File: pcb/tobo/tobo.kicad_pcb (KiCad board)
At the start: 2 copper layers, 57.5 x 61 mm, 97 parts, among them J1 Molex 538-54548-2272, J2 Conn_01x02_Pin, J4 Molex 538-54548-2472, J5 Conn_01x09_Pin, J6 Conn_01x09_Pin, J7 Conn_01x09_Pin, J8 Hroparts Elec TYPE-C-31-M-12, U1 TS5A23167, U10 5015, U11 5015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

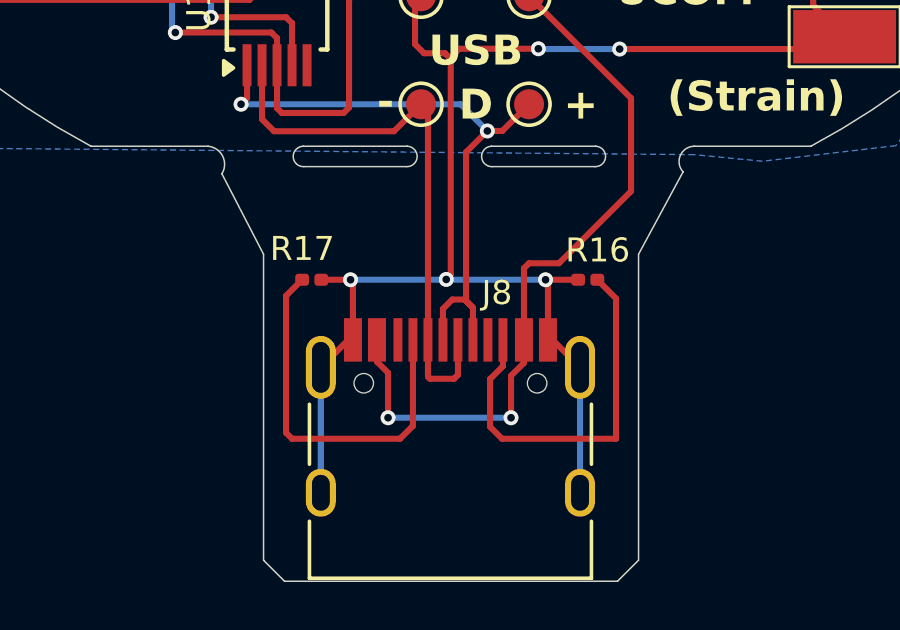
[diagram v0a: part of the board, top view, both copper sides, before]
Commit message: Cleared edges of USB board
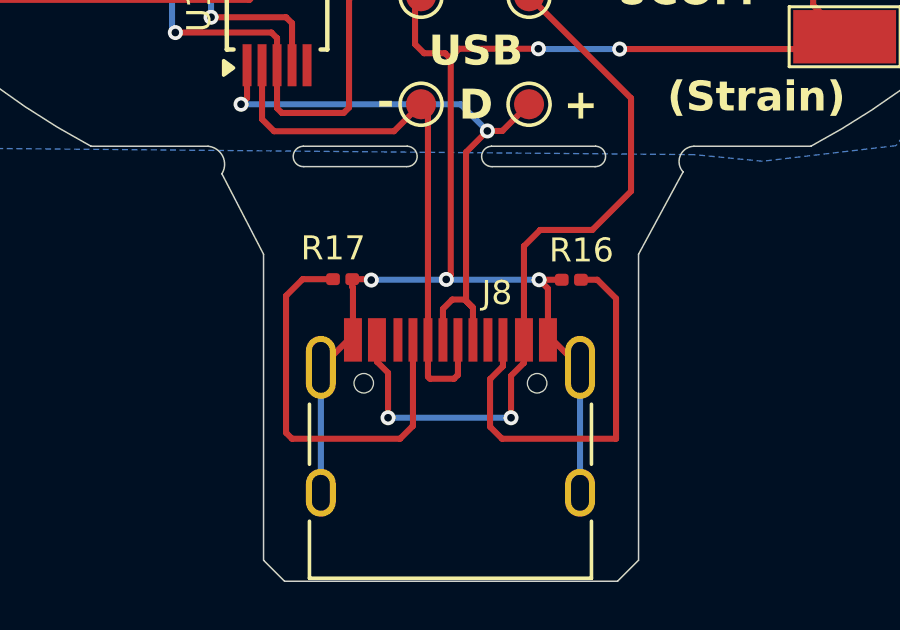
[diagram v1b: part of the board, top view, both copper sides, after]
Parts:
- moved R17 1.03 mm to (136.4, 116.9)
- moved R16 0.55 mm to (144.0, 117.0)
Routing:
- net GND: track 195.3 -> 193.8 mm
- net Net-(J8-CC1): track 12.7 -> 13.7 mm
- net Net-(J8-CC2): track 13.0 -> 13.5 mm
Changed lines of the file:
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@@
 	(footprint "Resistor_SMD:R_0201_0603Metric"
 		(layer "F.Cu")
-		(at 135.355 116.95)
+		(at 136.385 116.93)
 		(descr "Resistor SMD 0201 (0603 Metric), square (rectangular) end terminal, IPC_7351 nominal, (Body size source: https://www.vishay.com/docs/20052/crcw0201e3.pdf), generated with kicad-footprint-generator")
 		(tags "resistor")
@@
 	(footprint "Resistor_SMD:R_0201_0603Metric"
 		(layer "F.Cu")
-		(at 144.555 116.95 180)
+		(at 144.01 116.95 180)
 		(descr "Resistor SMD 0201 (0603 Metric), square (rectangular) end terminal, IPC_7351 nominal, (Body size source: https://www.vishay.com/docs/20052/crcw0201e3.pdf), generated with kicad-footprint-generator")
 		(tags "resistor")
@@
 	)
 	(segment
-		(start 136.73 118.955)
-		(end 136.73 117.03)
+		(start 136.705 117.185)
+		(end 136.705 116.93)
 		(width 0.2032)
 		(layer "F.Cu")
@@
 	)
 	(segment
+		(start 137.31 116.93)
+		(end 137.34 116.96)
+		(width 0.2032)
+		(layer "F.Cu")
+		(net 44)
+	)
+	(segment
 		(start 135.5 103.035)
 		(end 134.7 103.035)
@@
 	)
 	(segment
-		(start 135.675 116.95)
-		(end 136.65 116.95)
-		(width 0.2032)
-		(layer "F.Cu")
-		(net 44)
-	)
-	(segment
 		(start 131.11 78.63)
 		(end 145.849999 78.63)
@@
 	)
 	(segment
-		(start 136.73 117.03)
-		(end 136.65 116.95)
-		(width 0.2032)
-		(layer "F.Cu")
-		(net 44)
-	)
-	(segment
 		(start 136.7 107.5)
 		(end 139 107.5)
@@
 	(segment
 		(start 143.23 118.955)
-		(end 143.23 117.03)
+		(end 143.23 117.246)
 		(width 0.2032)
 		(layer "F.Cu")
@@
 	)
 	(segment
-		(start 153.12 108.85)
-		(end 152.71 109.26)
+		(start 142.934 116.95)
+		(end 143.69 116.95)
 		(width 0.2032)
 		(layer "F.Cu")
@@
 	)
 	(segment
-		(start 135.5 100.9)
-		(end 136.4 100)
+		(start 153.12 108.85)
+		(end 152.71 109.26)
 		(width 0.2032)
 		(layer "F.Cu")
@@
 	)
 	(segment
-		(start 144.235 116.95)
-		(end 143.15 116.95)
+		(start 135.5 100.9)
+		(end 136.4 100)
 		(width 0.2032)
 		(layer "F.Cu")
@@
 	)
 	(segment
+		(start 136.705 116.93)
+		(end 137.31 116.93)
+		(width 0.2032)
+		(layer "F.Cu")
+		(net 44)
+	)
+	(segment
 		(start 122.775 99.565)
 		(end 122.8 99.54)
@@
 	)
 	(segment
+		(start 136.73 118.955)
+		(end 136.73 117.21)
+		(width 0.2032)
+		(layer "F.Cu")
+		(net 44)
+	)
+	(segment
 		(start 122.035 84.8)
 		(end 122.035 85.7)
@@
 	)
 	(segment
-		(start 143.23 117.03)
-		(end 143.15 116.95)
-		(width 0.2032)
-		(layer "F.Cu")
-		(net 44)
-	)
-	(segment
 		(start 135.5 100.9)
 		(end 133.7 100.9)
@@
 	)
 	(segment
+		(start 143.23 117.246)
+		(end 142.934 116.95)
+		(width 0.2032)
+		(layer "F.Cu")
+		(net 44)
+	)
+	(segment
 		(start 133.9 103.035)
 		(end 134.7 103.035)
@@
 	)
 	(segment
+		(start 136.73 117.21)
+		(end 136.705 117.185)
+		(width 0.2032)
+		(layer "F.Cu")
+		(net 44)
+	)
+	(segment
 		(start 119.43 91.07)
 		(end 122 91.07)
@@
 	)
 	(via
-		(at 143.15 116.95)
+		(at 142.934 116.95)
 		(size 0.5)
 		(drill 0.254)
@@
 	)
 	(via
-		(at 136.65 116.95)
+		(at 137.34 116.96)
 		(size 0.5)
 		(drill 0.254)
@@
 	)
 	(segment
+		(start 137.34 116.96)
+		(end 137.35 116.95)
+		(width 0.2032)
+		(layer "B.Cu")
+		(net 44)
+	)
+	(segment
 		(start 135.5 100.9)
 		(end 135.5 101)
@@
 	)
 	(segment
-		(start 142.91 109.25)
-		(end 142.92 109.26)
+		(start 137.35 116.95)
+		(end 139.83 116.95)
 		(width 0.2032)
 		(layer "B.Cu")
@@
 	)
 	(segment
-		(start 143.15 116.95)
-		(end 139.85 116.95)
+		(start 142.91 109.25)
+		(end 142.92 109.26)
 		(width 0.2032)
 		(layer "B.Cu")
@@
 	)
 	(segment
-		(start 139.83 116.95)
-		(end 136.65 116.95)
+		(start 124.7 88.5)
+		(end 124.7 89.9)
 		(width 0.2032)
 		(layer "B.Cu")
@@
 	)
 	(segment
-		(start 139.84 116.94)
-		(end 139.83 116.95)
+		(start 144.3 124.05)
+		(end 144.3 119.87)
 		(width 0.2032)
 		(layer "B.Cu")
@@
 	)
 	(segment
-		(start 124.7 88.5)
-		(end 124.7 89.9)
+		(start 121.95 82.35)
+		(end 121.95 86.75)
 		(width 0.2032)
 		(layer "B.Cu")
@@
 	)
 	(segment
-		(start 144.3 124.05)
-		(end 144.3 119.87)
+		(start 136.4 84.7)
+		(end 136.4 89.7)
 		(width 0.2032)
 		(layer "B.Cu")
@@
 	)
 	(segment
-		(start 121.95 82.35)
-		(end 121.95 86.75)
+		(start 139.85 116.95)
+		(end 139.84 116.94)
 		(width 0.2032)
 		(layer "B.Cu")
@@
 	)
 	(segment
-		(start 136.4 84.7)
-		(end 136.4 89.7)
+		(start 142.934 116.95)
+		(end 139.85 116.95)
 		(width 0.2032)
 		(layer "B.Cu")
@@
 	)
 	(segment
-		(start 139.85 116.95)
-		(end 139.84 116.94)
-		(width 0.2032)
-		(layer "B.Cu")
-		(net 44)
-	)
-	(segment
 		(start 130.7 108.6)
 		(end 130.81 108.71)
@@
 	)
 	(segment
+		(start 139.83 116.95)
+		(end 139.84 116.94)
+		(width 0.2032)
+		(layer "B.Cu")
+		(net 44)
+	)
+	(segment
 		(start 136.68 84.42)
 		(end 136.4 84.7)
@@
 	)
 	(segment
+		(start 142.43 115.83)
+		(end 142.97 115.29)
+		(width 0.2032)
+		(layer "F.Cu")
+		(net 89)
+	)
+	(segment
 		(start 137.53 119.68)
 		(end 137.53 118.955)
@@
 	)
 	(segment
-		(start 143.6 116.4)
+		(start 144.71 115.29)
 		(end 146 114)
 		(width 0.2032)
@@
 	)
 	(segment
-		(start 142.43 116.57)
-		(end 142.6 116.4)
+		(start 134.7 103.675)
+		(end 135.5 103.675)
 		(width 0.2032)
 		(layer "F.Cu")
@@
 	)
 	(segment
-		(start 142.6 116.4)
-		(end 143.6 116.4)
+		(start 146 110.9)
+		(end 142.6 107.5)
 		(width 0.2032)
 		(layer "F.Cu")
@@
 	)
 	(segment
-		(start 134.7 103.675)
-		(end 135.5 103.675)
+		(start 142.43 118.955)
+		(end 142.43 115.83)
 		(width 0.2032)
 		(layer "F.Cu")
@@
 	)
 	(segment
-		(start 142.43 118.955)
-		(end 142.43 116.57)
+		(start 146 114)
+		(end 146 110.9)
 		(width 0.2032)
 		(layer "F.Cu")
@@
 	)
 	(segment
-		(start 137.9 120.05)
-		(end 137.53 119.68)
+		(start 142.97 115.29)
+		(end 144.71 115.29)
 		(width 0.2032)
 		(layer "F.Cu")
@@
 	)
 	(segment
-		(start 146 110.9)
-		(end 142.6 107.5)
+		(start 137.9 120.05)
+		(end 137.53 119.68)
 		(width 0.2032)
 		(layer "F.Cu")
@@
 	)
 	(segment
-		(start 146 114)
-		(end 146 110.9)
-		(width 0.2032)
-		(layer "F.Cu")
-		(net 89)
-	)
-	(segment
 		(start 134.7 105.4)
 		(end 134.7 103.675)
@@
 	)
 	(segment
-		(start 134.5 122.05)
-		(end 134.7 122.25)
+		(start 134.5 117.485)
+		(end 135.055 116.93)
 		(width 0.2032)
 		(layer "F.Cu")
@@
 	)
 	(segment
-		(start 138.73 121.82)
-		(end 138.73 118.955)
+		(start 135.055 116.93)
+		(end 136.065 116.93)
 		(width 0.2032)
 		(layer "F.Cu")
@@
 	)
 	(segment
-		(start 138.3 122.25)
-		(end 138.73 121.82)
+		(start 138.73 121.82)
+		(end 138.3 122.25)
 		(width 0.2032)
 		(layer "F.Cu")
@@
 	)
 	(segment
-		(start 135.035 116.95)
-		(end 134.5 117.485)
+		(start 138.3 122.25)
+		(end 134.7 122.25)
 		(width 0.2032)
 		(layer "F.Cu")
@@
 	(segment
 		(start 134.7 122.25)
-		(end 138.3 122.25)
+		(end 134.5 122.05)
 		(width 0.2032)
 		(layer "F.Cu")
@@
 	)
 	(segment
-		(start 134.5 117.485)
-		(end 134.5 122.05)
+		(start 134.5 122.05)
+		(end 134.5 117.485)
 		(width 0.2032)
 		(layer "F.Cu")
@@
 	)
 	(segment
-		(start 141.3 120.2624)
-		(end 141.73 119.8324)
+		(start 138.73 118.955)
+		(end 138.73 121.82)
 		(width 0.2032)
 		(layer "F.Cu")
-		(net 95)
+		(net 94)
 	)
 	(segment
-		(start 144.875 116.95)
-		(end 145.5 117.575)
+		(start 141.3 120.2624)
+		(end 141.73 119.8324)
 		(width 0.2032)
 		(layer "F.Cu")
@@
 	)
 	(segment
+		(start 144.875 116.95)
+		(end 144.33 116.95)
+		(width 0.2032)
+		(layer "F.Cu")
+		(net 95)
+	)
+	(segment
 		(start 145.5 122.25)
 		(end 141.7 122.25)
@@
 		(width 0.2032)
 		(layer "F.Cu")
+		(net 95)
+	)
+	(segment
+		(start 145.5 117.575)
+		(end 144.875 116.95)
+		(width 0.2032)
+		(layer "F.Cu")

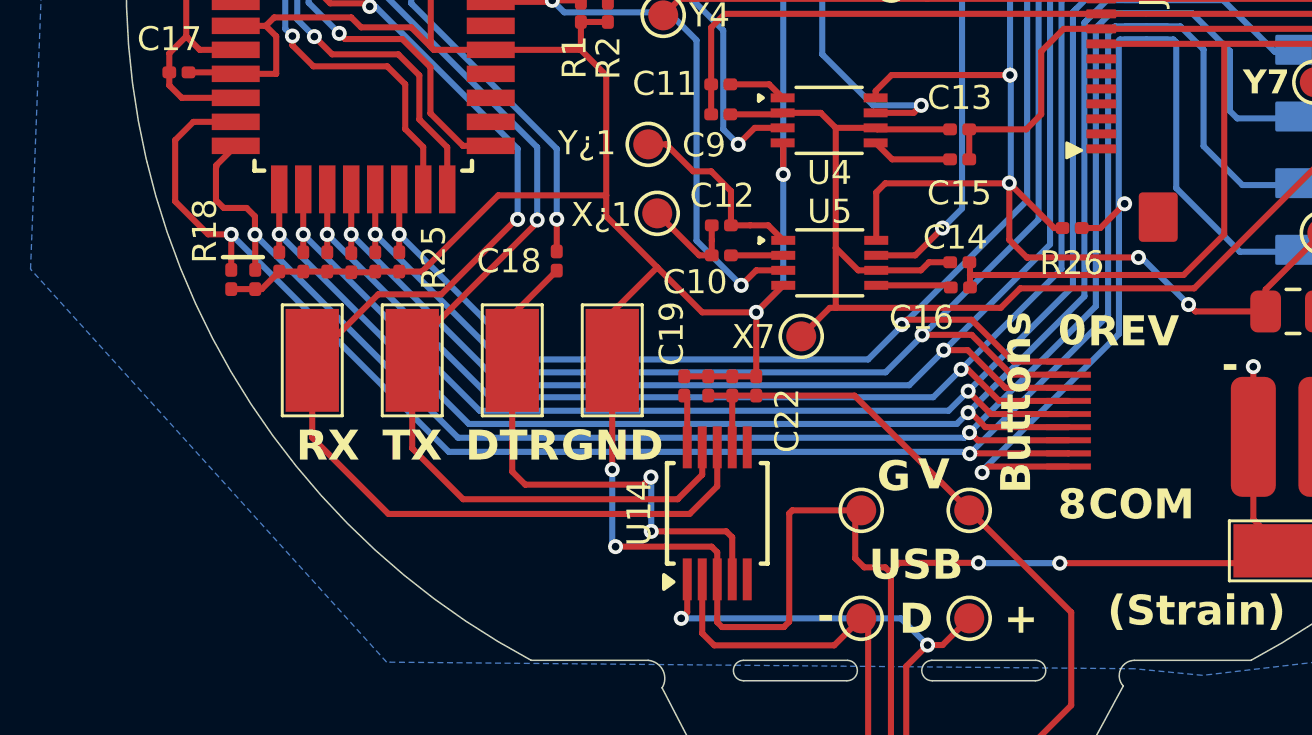
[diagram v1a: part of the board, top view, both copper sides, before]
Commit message: Internal pull-ups for the buttons. May as well.
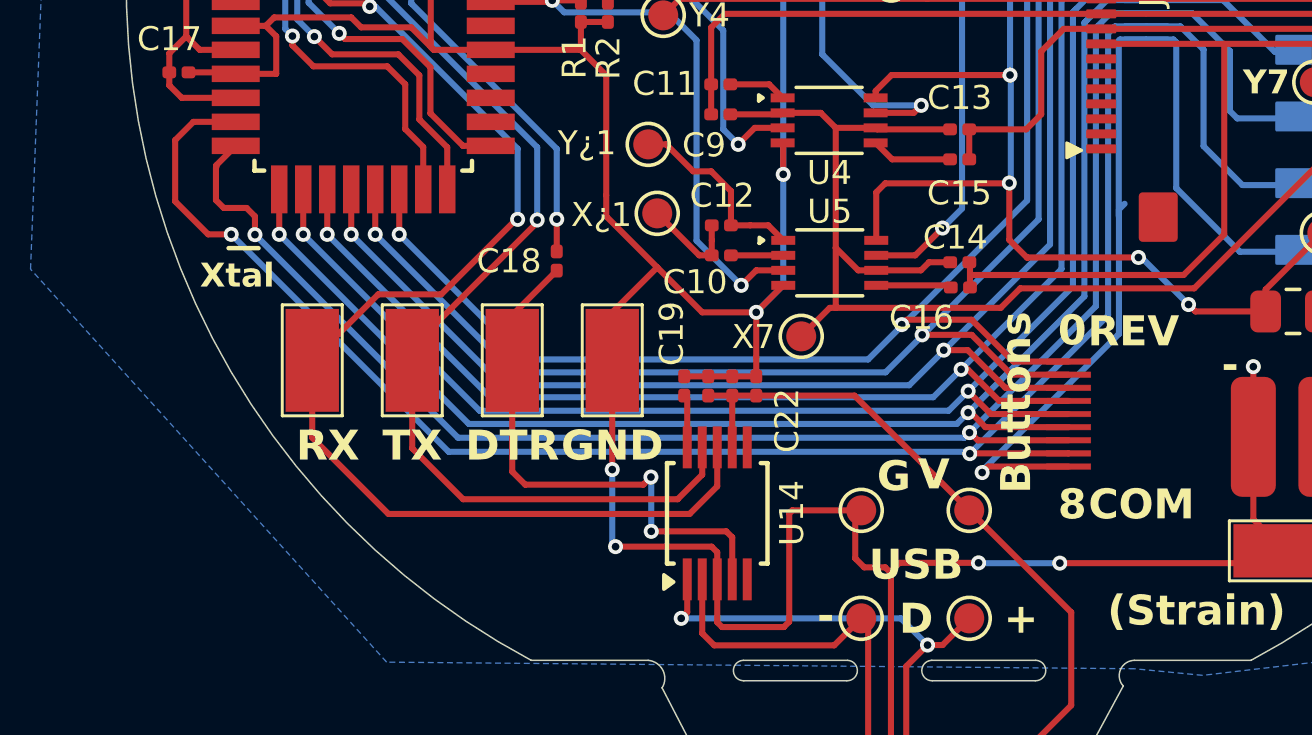
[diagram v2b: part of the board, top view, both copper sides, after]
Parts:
- removed R18, R19, R20, R21, R22, R23, R24, R25, R26: 1K, Resistor_SMD:R_0201_0603Metric
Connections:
- J5 pad 9: /BTNC -> GND
- J6 pad 9: /BTNC -> GND
- J7 pad 9: /BTNC -> GND
- S1 pad 1: /BTNC -> GND
- S1 pad 3: /BTNC -> GND
- S2 pad 1: /BTNC -> GND
- S2 pad 3: /BTNC -> GND
- S3 pad 1: /BTNC -> GND
- S3 pad 3: /BTNC -> GND
- S4 pad 1: /BTNC -> GND
- S4 pad 3: /BTNC -> GND
- S5 pad 1: /BTNC -> GND
- S5 pad 3: /BTNC -> GND
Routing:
- net /BTNC: track 87.2 -> 0.00 mm, vias 9 -> 0
- net GND: track 193.8 -> 265.4 mm, vias 14 -> 22
- net +BATT: track 102.7 -> 100.3 mm
- net /BTN7: track 65.9 -> 64.7 mm
- net /BTN6: track 61.0 -> 59.9 mm
- net /BTN2: track 76.5 -> 75.9 mm
- net /BTN5: track 54.9 -> 54.3 mm
- net /BTN4: track 76.8 -> 76.2 mm
- net /BTN3: track 75.9 -> 75.3 mm
- net /BTN1: track 75.2 -> 74.6 mm
- net /BTN0: track 75.4 -> 74.8 mm
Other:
- board text added: "Xtal"

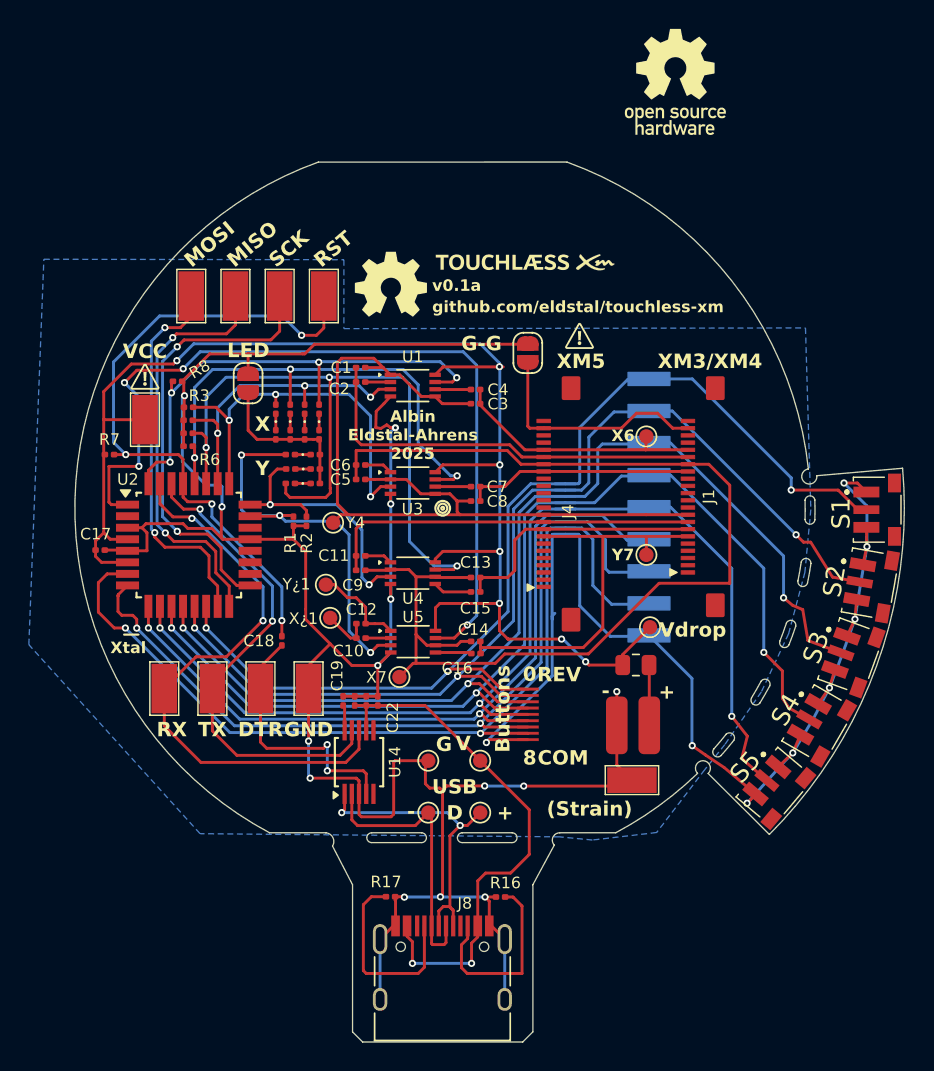
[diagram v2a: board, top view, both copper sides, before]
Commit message: Untented all the vias in order to allow a crystal
We don't actually need one, but if you mess up burning
the bootloader, you may need to hold a crystal to the contacts
in order to correct the programming.

In Kicad 9, we may be able to re-tent all the vias and untent these.
That would be nice.
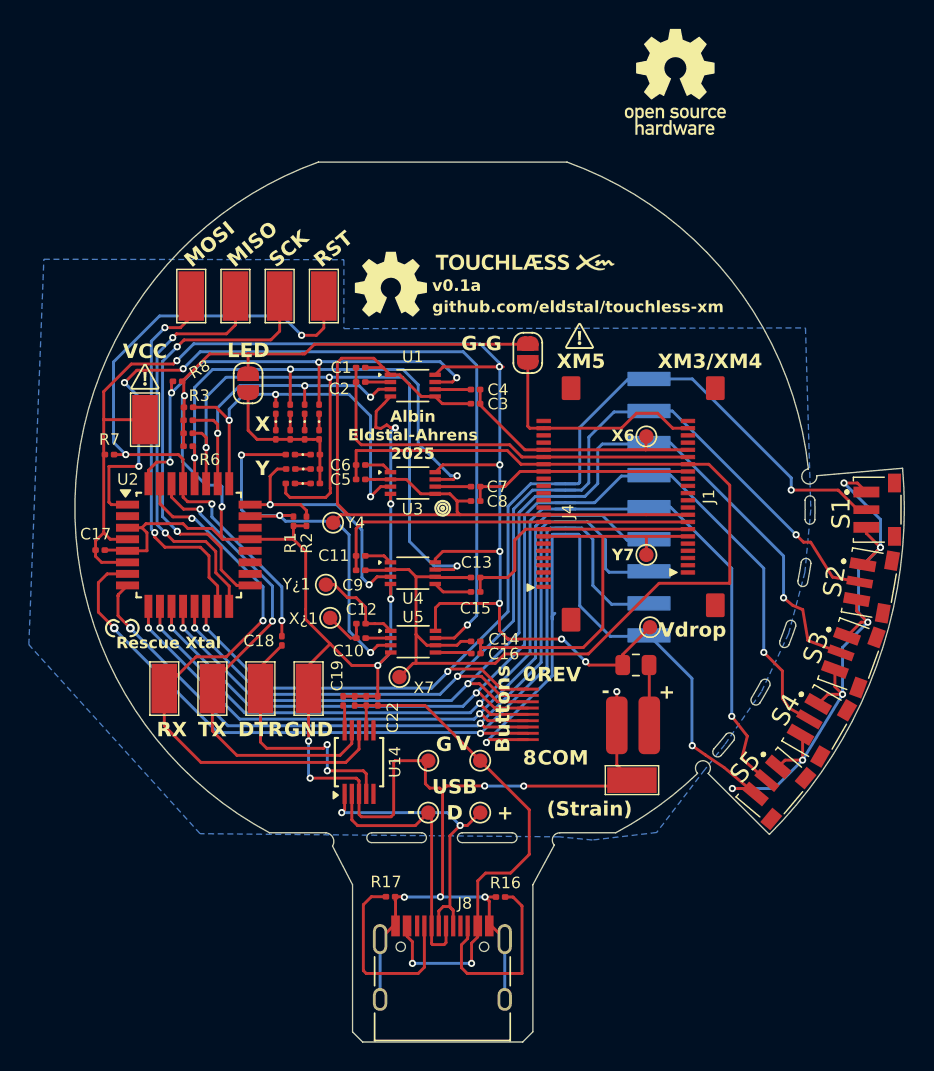
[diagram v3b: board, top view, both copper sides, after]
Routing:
- net GND: track 265.4 -> 273.6 mm
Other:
- board text added: "Rescue Xtal"
- board text removed: "Xtal"
